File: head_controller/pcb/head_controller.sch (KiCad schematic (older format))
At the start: 17 parts, among them P1 HEADER_02X08_SMD

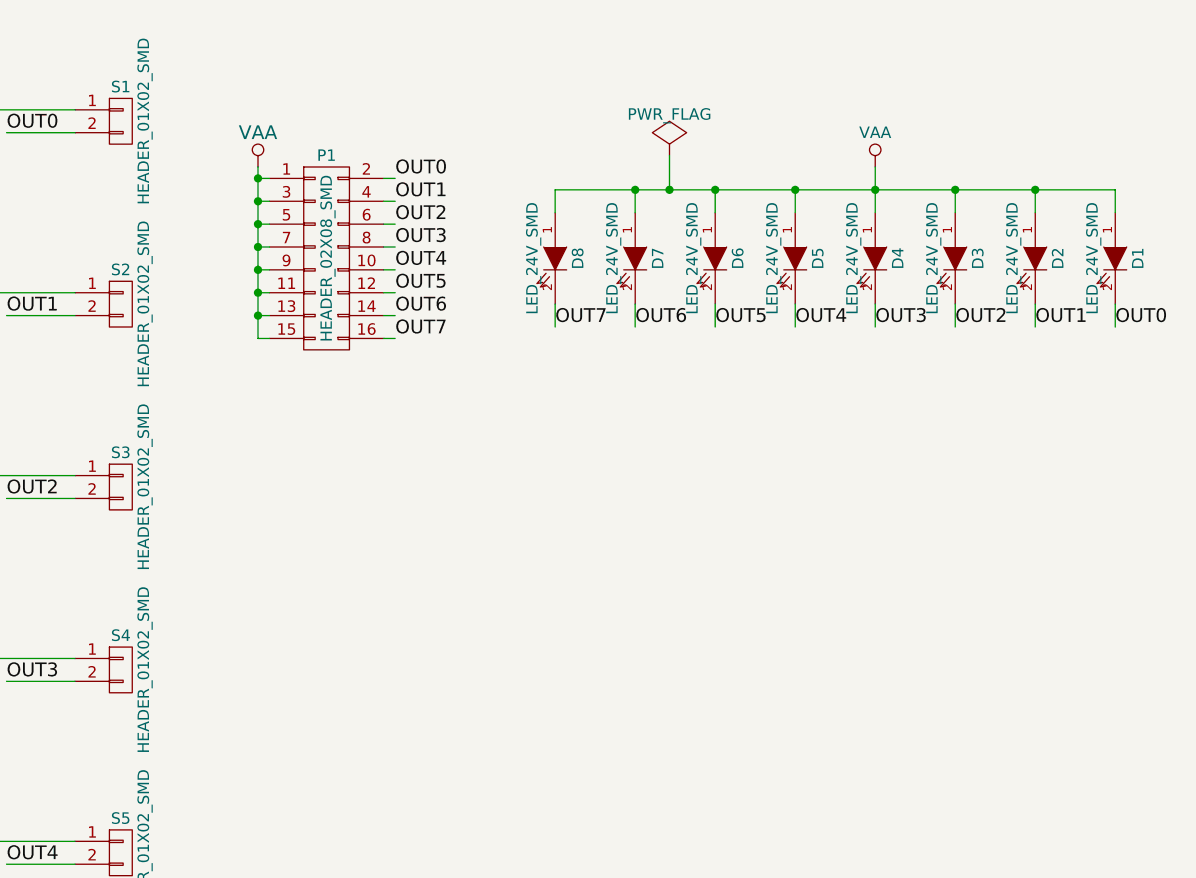
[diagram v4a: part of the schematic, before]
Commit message: Added footprints.
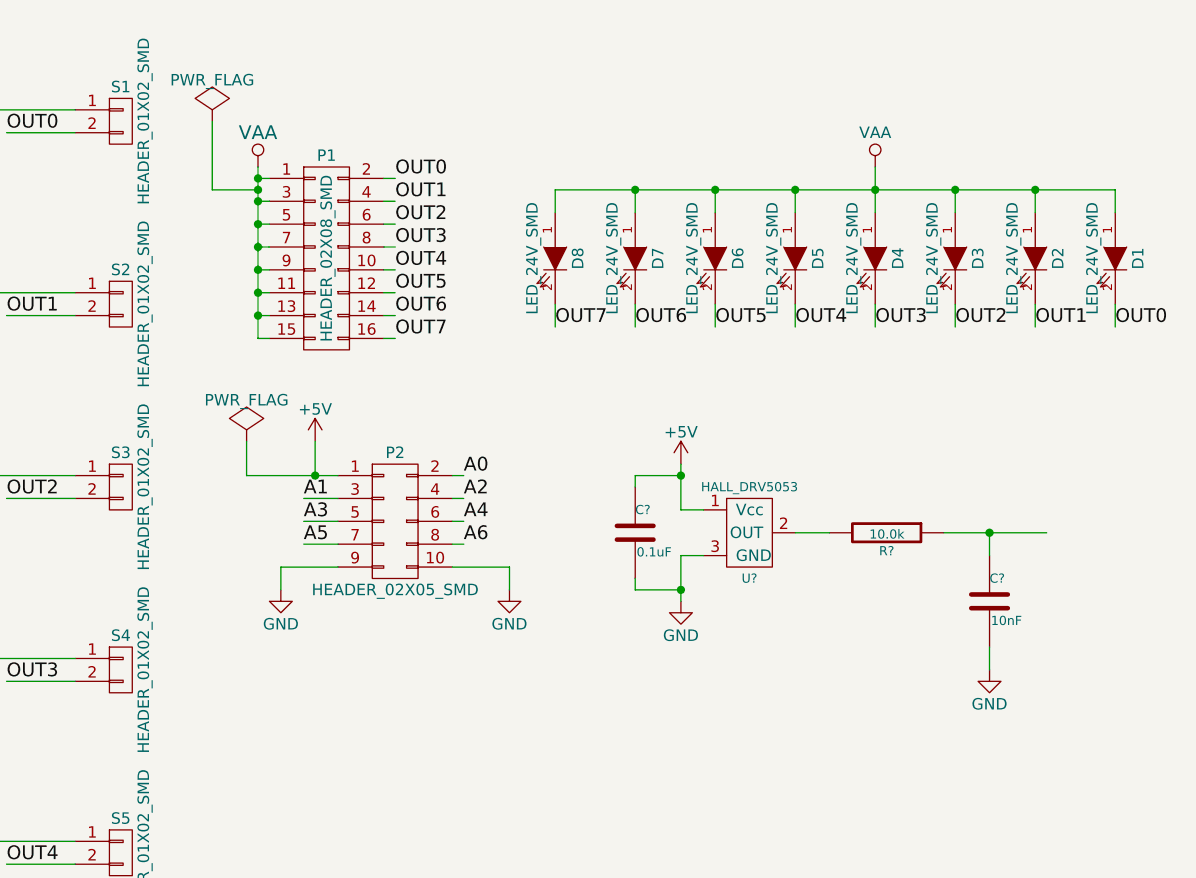
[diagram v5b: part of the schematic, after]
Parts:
- added C?: 0.1uF, head_controller:SM1210, symbol 0.1uF
- added C?: 10nF, head_controller:SM1210, symbol 10nF
- added P2: HEADER_02X05_SMD, head_controller:HEADER_02x05_SMD, symbol HEADER_02X05_SMD
- added R?: 10.0k, head_controller:SM1210, symbol 10.0k
- added U?: HALL_DRV5053, head_controller:SOT-23-3, symbol HALL_DRV5053
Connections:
- new net: R?.2, U?.2 (OUT)
- new net: C?.1, R?.1
- new net +5V: C?.1, P2.1 (P1), U?.1 (Vcc)
- new net A0: P2.2 (P2)
- new net A1: P2.3 (P3)
- new net A2: P2.4 (P4)
- new net A3: P2.5 (P5)
- new net A4: P2.6 (P6)
- new net A5: P2.7 (P7)
- new net A6: P2.8 (P8)
- new net GND: C?.2, C?.2, P2.10 (P10), P2.9 (P9), U?.3 (GND)
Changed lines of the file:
@@
 L PWR_FLAG #FLG04
 U 1 1 553ED439
-P 3750 1200
-F 0 "#FLG04" H 3750 1295 50  0001 C CNN
-F 1 "PWR_FLAG" H 3750 1380 50  0000 C CNN
-F 2 "" H 3750 1200 60  0000 C CNN
-F 3 "" H 3750 1200 60  0000 C CNN
-	1    3750 1200
-	1    0    0    -1
-$EndComp
-Wire Wire Line
-	3750 1200 3750 1350
-Connection ~ 3750 1350
+P 1750 1050
+F 0 "#FLG04" H 1750 1145 50  0001 C CNN
+F 1 "PWR_FLAG" H 1750 1230 50  0000 C CNN
+F 2 "" H 1750 1050 60  0000 C CNN
+F 3 "" H 1750 1050 60  0000 C CNN
+	1    1750 1050
+	1    0    0    -1
+$EndComp
 Wire Wire Line
 	2500 2000 2550 2000
@@
 	1    0    0    -1
 $EndComp
+$Comp
+L HALL_DRV5053 U?
+U 1 1 553FCBDD
+P 4100 2850
+F 0 "U?" H 4100 2650 40  0000 C CNN
+F 1 "HALL_DRV5053" H 4100 3050 40  0000 C CNN
+F 2 "head_controller:SOT-23-3" H 4000 2550 60  0001 C CNN
+F 3 "" H 4100 2850 60  0000 C CNN
+F 4 "Digikey" H 4200 2750 60  0001 C CNN "Vendor"
+F 5 "296-38460-1-ND" H 4300 2850 60  0001 C CNN "PartNumber"
+F 6 "IC HALL SENSOR 9mT" H 4400 2950 60  0001 C CNN "Description"
+	1    4100 2850
+	1    0    0    -1
+$EndComp
+$Comp
+L HEADER_02X05_SMD P2
+U 1 1 553FDA31
+P 2550 2800
+F 0 "P2" H 2550 3100 50  0000 C CNN
+F 1 "HEADER_02X05_SMD" H 2550 2500 50  0000 C CNN
+F 2 "head_controller:HEADER_02x05_SMD" H 2550 1600 60  0001 C CNN
+F 3 "" H 2550 1600 60  0000 C CNN
+F 4 "digikey" H 2650 3200 60  0001 C CNN "Vendor"
+F 5 "S9185-ND" H 2750 3300 60  0001 C CNN "PartNumber"
+F 6 "CONN_HEADR_2.54MM_10POS_GOLD_SMD" H 2850 3400 60  0001 C CNN "Description"
+	1    2550 2800
+	1    0    0    -1
+$EndComp
+Wire Wire Line
+	1750 1050 1750 1350
+Wire Wire Line
+	1750 1350 1950 1350
+Connection ~ 1950 1350
+$Comp
+L +5V #PWR?
+U 1 1 553FE25A
+P 2200 2450
+F 0 "#PWR?" H 2200 2300 50  0001 C CNN
+F 1 "+5V" H 2200 2590 50  0000 C CNN
+F 2 "" H 2200 2450 60  0000 C CNN
+F 3 "" H 2200 2450 60  0000 C CNN
+	1    2200 2450
+	1    0    0    -1
+$EndComp
+Wire Wire Line
+	2200 2450 2200 2600
+Wire Wire Line
+	1900 2600 2300 2600
+$Comp
+L PWR_FLAG #FLG?
+U 1 1 553FE2E0
+P 1900 2450
+F 0 "#FLG?" H 1900 2545 50  0001 C CNN
+F 1 "PWR_FLAG" H 1900 2630 50  0000 C CNN
+F 2 "" H 1900 2450 60  0000 C CNN
+F 3 "" H 1900 2450 60  0000 C CNN
+	1    1900 2450
+	1    0    0    -1
+$EndComp
+Wire Wire Line
+	1900 2450 1900 2600
+Connection ~ 2200 2600
+Wire Wire Line
+	2800 2600 2850 2600
+Wire Wire Line
+	2800 2700 2850 2700
+Wire Wire Line
+	2800 2800 2850 2800
+Wire Wire Line
+	2800 2900 2850 2900
+Wire Wire Line
+	2800 3000 3050 3000
+Wire Wire Line
+	2300 2700 2150 2700
+Wire Wire Line
+	2300 2800 2150 2800
+Wire Wire Line
+	2300 2900 2150 2900
+Wire Wire Line
+	2050 3000 2300 3000
+Text Label 2850 2600 0    60   ~ 0
+A0
+Text Label 2150 2700 0    60   ~ 0
+A1
+Text Label 2850 2700 0    60   ~ 0
+A2
+Text Label 2150 2800 0    60   ~ 0
+A3
+Text Label 2850 2800 0    60   ~ 0
+A4
+Text Label 2150 2900 0    60   ~ 0
+A5
+Text Label 2850 2900 0    60   ~ 0
+A6
+$Comp
+L GND #PWR?
+U 1 1 553FEAB2
+P 2050 3100
+F 0 "#PWR?" H 2050 2850 50  0001 C CNN
+F 1 "GND" H 2050 2950 50  0000 C CNN
+F 2 "" H 2050 3100 60  0000 C CNN
+F 3 "" H 2050 3100 60  0000 C CNN
+	1    2050 3100
+	1    0    0    -1
+$EndComp
+$Comp
+L GND #PWR?
+U 1 1 553FEAD9
+P 3050 3100
+F 0 "#PWR?" H 3050 2850 50  0001 C CNN
+F 1 "GND" H 3050 2950 50  0000 C CNN
+F 2 "" H 3050 3100 60  0000 C CNN
+F 3 "" H 3050 3100 60  0000 C CNN
+	1    3050 3100
+	1    0    0    -1
+$EndComp
+Wire Wire Line
+	3050 3000 3050 3100
+Wire Wire Line
+	2050 3000 2050 3100
+$Comp
+L 0.1uF C?
+U 1 1 553FED9B
+P 3600 2850
+F 0 "C?" H 3600 2950 40  0000 L CNN
+F 1 "0.1uF" H 3606 2765 40  0000 L CNN
+F 2 "head_controller:SM1210" H 3638 2700 30  0001 C CNN
+F 3 "" H 3600 2850 60  0000 C CNN
+F 4 "digikey" H 3700 3050 60  0001 C CNN "Vendor"
+F 5 "478-3586-1-ND" H 3800 3150 60  0001 C CNN "PartNumber"
+F 6 "CAP CER 0.1UF 50V 10% X7R 1210" H 3900 3250 60  0001 C CNN "Description"
+	1    3600 2850
+	1    0    0    -1
+$EndComp
+$Comp
+L GND #PWR?
+U 1 1 553FEDDB
+P 3800 3150
+F 0 "#PWR?" H 3800 2900 50  0001 C CNN
+F 1 "GND" H 3800 3000 50  0000 C CNN
+F 2 "" H 3800 3150 60  0000 C CNN
+F 3 "" H 3800 3150 60  0000 C CNN
+	1    3800 3150
+	1    0    0    -1
+$EndComp
+Wire Wire Line
+	3600 3050 3600 3100
+Wire Wire Line
+	3600 3100 3800 3100
+Wire Wire Line
+	3800 2950 3800 3150
+Wire Wire Line
+	3800 2950 3900 2950
+Connection ~ 3800 3100
+$Comp
+L +5V #PWR?
+U 1 1 553FEF60
+P 3800 2550
+F 0 "#PWR?" H 3800 2400 50  0001 C CNN
+F 1 "+5V" H 3800 2690 50  0000 C CNN
+F 2 "" H 3800 2550 60  0000 C CNN
+F 3 "" H 3800 2550 60  0000 C CNN
+	1    3800 2550
+	1    0    0    -1
+$EndComp
+Wire Wire Line
+	3600 2650 3600 2600
+Wire Wire Line
+	3600 2600 3800 2600
+Wire Wire Line
+	3800 2550 3800 2750
+Wire Wire Line
+	3800 2750 3900 2750
+Connection ~ 3800 2600
+$Comp
+L 10.0k R?
+U 1 1 553FF8F8
+P 4700 2850
+F 0 "R?" V 4780 2850 40  0000 C CNN
+F 1 "10.0k" V 4707 2851 40  0000 C CNN
+F 2 "head_controller:SM1210" V 4630 2850 30  0001 C CNN
+F 3 "" H 4700 2850 30  0000 C CNN
+F 4 "digikey" V 4880 2950 60  0001 C CNN "Vendor"
+F 5 "P10.0KAACT-ND" V 4980 3050 60  0001 C CNN "PartNumber"
+F 6 "RES SMD 10.0K OHM 1% 1/2W 1210" V 5080 3150 60  0001 C CNN "Description"
+	1    4700 2850
+	0    1    1    0
+$EndComp
+$Comp
+L 10nF C?
+U 1 1 553FFE8D
+P 5150 3150
+F 0 "C?" H 5150 3250 40  0000 L CNN
+F 1 "10nF" H 5156 3065 40  0000 L CNN
+F 2 "head_controller:SM1210" H 5188 3000 30  0001 C CNN
+F 3 "" H 5150 3150 60  0000 C CNN
+F 4 "digikey" H 5250 3350 60  0001 C CNN "Vendor"
+F 5 "399-1266-1-ND" H 5350 3450 60  0001 C CNN "PartNumber"
+F 6 "CAP CER 10000PF 50V 5% NP0 1210" H 5450 3550 60  0001 C CNN "Description"
+	1    5150 3150
+	1    0    0    -1
+$EndComp
+$Comp
+L GND #PWR?
+U 1 1 553FFED1
+P 5150 3450
+F 0 "#PWR?" H 5150 3200 50  0001 C CNN
+F 1 "GND" H 5150 3300 50  0000 C CNN
+F 2 "" H 5150 3450 60  0000 C CNN
+F 3 "" H 5150 3450 60  0000 C CNN
+	1    5150 3450
+	1    0    0    -1
+$EndComp
+Wire Wire Line
+	4300 2850 4450 2850
+Wire Wire Line
+	4950 2850 5400 2850
+Wire Wire Line
+	5150 2950 5150 2850
+Connection ~ 5150 2850
+Wire Wire Line
+	5150 3350 5150 3450
 $EndSCHEMATC

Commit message: Initial board layout.
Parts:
- removed C?: 10nF, head_controller:SM1210, symbol 10nF
- removed R?: 10.0k, head_controller:SM1210, symbol 10.0k
- removed S8: LEE_VALVE_3WAY, head_controller:LEE_VALVE_PLUG_IN, symbol LEE_VALVE_3WAY
- added C10, C12, C13, C15, C16, C18, C19, C21, C3, C4, C6, C7, C9: 0.1uF, head_controller:SM1210, symbol 0.1uF
- added C11, C14, C17, C2, C20, C5, C8: 8.2nF, head_controller:SM1210, symbol 8.2nF
- added R1, R2, R3, R4, R5, R6, R7: 200k, head_controller:SM1210, symbol 200k
- added S8: LEE_VALVE_PLUG_IN, head_controller:LEE_VALVE_PLUG_IN, symbol LEE_VALVE_PLUG_IN
- added U10, U12, U14, U2, U4, U6, U8: MAX4215, head_controller:SOIC_8_N, symbol MAX4215
- added U11, U13, U3, U5, U7, U9: HALL_DRV5053, head_controller:SOT-23-3, symbol HALL_DRV5053
- gave numbers to parts that had none: 2
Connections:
- net +5V: now also C10.1, C12.1, C13.1, C15.1, C16.1, C18.1, C19.1, C21.1, C3.1, C4.1, C6.1, C7.1, C9.1, U10.7 (Vcc), U10.8 (EN), U11.1 (Vcc), U12.7 (Vcc), U12.8 (EN), U13.1 (Vcc), U14.7 (Vcc), U14.8 (EN), U2.7 (Vcc), U2.8 (EN), U3.1 (Vcc), U4.7 (Vcc), U4.8 (EN), U5.1 (Vcc), U6.7 (Vcc), U6.8 (EN), U7.1 (Vcc), U8.7 (Vcc), U8.8 (EN), U9.1 (Vcc)
- net A0: now also U2.6 (OUT)
- net A1: now also U4.6 (OUT)
- net A2: now also U6.6 (OUT)
- net A3: now also U8.6 (OUT)
- net A4: now also U10.6 (OUT)
- net A5: now also U12.6 (OUT)
- net A6: now also U14.6 (OUT)
- net GND: now also C10.2, C11.2, C12.2, C13.2, C14.2, C15.2, C16.2, C17.2, C18.2, C19.2, C2.2, C20.2, C21.2, C3.2, C4.2, C5.2, C6.2, C7.2, C8.2, C9.2, U10.2 (IN-), U10.4 (Vee), U11.3 (GND), U12.2 (IN-), U12.4 (Vee), U13.3 (GND), U14.2 (IN-), U14.4 (Vee), U2.2 (IN-), U2.4 (Vee), U3.3 (GND), U4.2 (IN-), U4.4 (Vee), U5.3 (GND), U6.2 (IN-), U6.4 (Vee), U7.3 (GND), U8.2 (IN-), U8.4 (Vee), U9.3 (GND)
- net OUT7: now also S8.2 (P2)
- net VAA: now also S8.1 (P1)
- net at U1.2 (OUT): now also R1.2
- new net: C2.1, R1.1, U2.3 (IN+)
- new net: R2.2, U3.2 (OUT)
- new net: C5.1, R2.1, U4.3 (IN+)
- new net: R3.2, U5.2 (OUT)
- new net: C8.1, R3.1, U6.3 (IN+)
- new net: R4.2, U7.2 (OUT)
- new net: C11.1, R4.1, U8.3 (IN+)
- new net: R5.2, U9.2 (OUT)
- new net: C14.1, R5.1, U10.3 (IN+)
- new net: R6.2, U11.2 (OUT)
- new net: C17.1, R6.1, U12.3 (IN+)
- new net: R7.2, U13.2 (OUT)
- new net: C20.1, R7.1, U14.3 (IN+)
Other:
- moved on the sheet: C1, U1
